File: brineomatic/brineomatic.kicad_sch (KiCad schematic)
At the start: 9 parts, among them J1 Conn_01x04_MountingPin

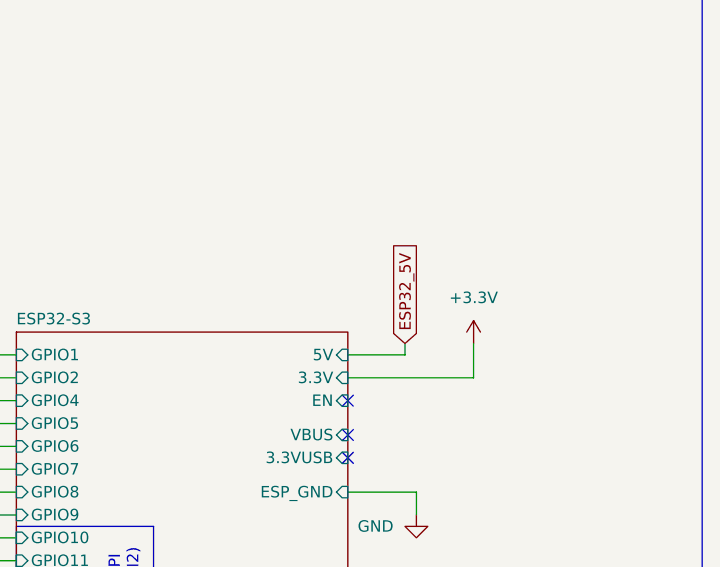
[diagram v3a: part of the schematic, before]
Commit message: 5v power supply is sorted.
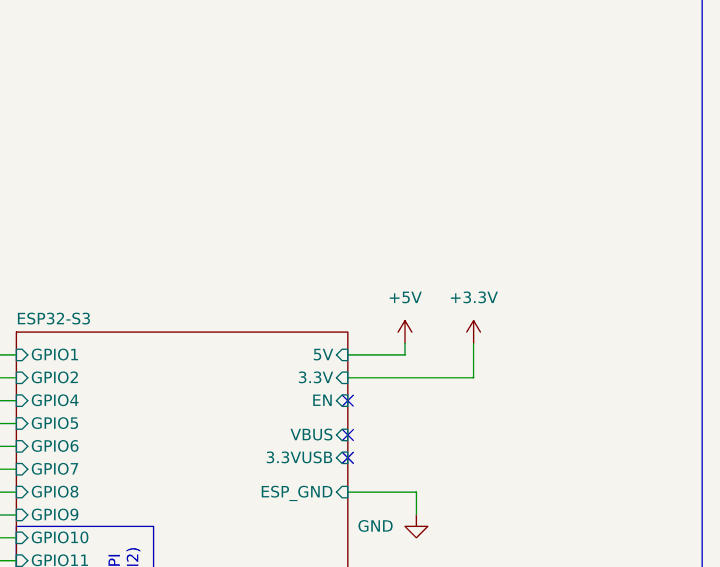
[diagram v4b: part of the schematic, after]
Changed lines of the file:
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@@
 		)
 	)
-	(global_label "ESP32_5V"
+	(global_label "SCL"
 		(shape input)
-		(at 241.3 69.85 90)
+		(at 195.58 96.52 180)
 		(fields_autoplaced yes)
 		(effects
@@
 				(size 1.27 1.27)
 			)
-			(justify left)
+			(justify right)
 		)
 		(property "Intersheetrefs" "${INTERSHEET_REFS}"
-			(at 241.3 57.5516 90)
-			(effects
-				(font
-					(size 1.27 1.27)
-				)
-				(justify left)
-				(hide yes)
-			)
-		)
-	)
-	(global_label "SCL"
+			(at 189.0872 96.52 0)
+			(effects
+				(font
+					(size 1.27 1.27)
+				)
+				(justify right)
+				(hide yes)
+			)
+		)
+	)
+	(global_label "GPIO48"
 		(shape input)
-		(at 195.58 96.52 180)
+		(at 45.72 175.26 0)
 		(fields_autoplaced yes)
 		(effects
@@
 				(size 1.27 1.27)
 			)
-			(justify right)
+			(justify left)
 		)
 		(property "Intersheetrefs" "${INTERSHEET_REFS}"
-			(at 189.0872 96.52 0)
-			(effects
-				(font
-					(size 1.27 1.27)
-				)
-				(justify right)
-				(hide yes)
-			)
-		)
-	)
-	(global_label "GPIO48"
+			(at 55.5995 175.26 0)
+			(effects
+				(font
+					(size 1.27 1.27)
+				)
+				(justify left)
+				(hide yes)
+			)
+		)
+	)
+	(global_label "SOLENOID3"
 		(shape input)
-		(at 45.72 175.26 0)
+		(at 162.56 91.44 0)
 		(fields_autoplaced yes)
 		(effects
@@
 		)
 		(property "Intersheetrefs" "${INTERSHEET_REFS}"
-			(at 55.5995 175.26 0)
+			(at 176.0076 91.44 0)
 			(effects
 				(font
@@
 		)
 	)
-	(global_label "SOLENOID3"
+	(global_label "TMC2209_RX"
 		(shape input)
-		(at 162.56 91.44 0)
+		(at 195.58 88.9 180)
 		(fields_autoplaced yes)
 		(effects
@@
 				(size 1.27 1.27)
 			)
-			(justify left)
+			(justify right)
 		)
 		(property "Intersheetrefs" "${INTERSHEET_REFS}"
-			(at 176.0076 91.44 0)
-			(effects
-				(font
-					(size 1.27 1.27)
-				)
-				(justify left)
-				(hide yes)
-			)
-		)
-	)
-	(global_label "TMC2209_RX"
+			(at 180.6207 88.9 0)
+			(effects
+				(font
+					(size 1.27 1.27)
+				)
+				(justify right)
+				(hide yes)
+			)
+		)
+	)
+	(global_label "GPIO5"
 		(shape input)
-		(at 195.58 88.9 180)
+		(at 195.58 78.74 180)
 		(fields_autoplaced yes)
 		(effects
@@
 		)
 		(property "Intersheetrefs" "${INTERSHEET_REFS}"
-			(at 180.6207 88.9 0)
+			(at 186.91 78.74 0)
 			(effects
 				(font
@@
 		)
 	)
-	(global_label "GPIO5"
+	(global_label "SOLENOID2"
 		(shape input)
-		(at 195.58 78.74 180)
+		(at 195.58 106.68 180)
 		(fields_autoplaced yes)
 		(effects
@@
 		)
 		(property "Intersheetrefs" "${INTERSHEET_REFS}"
-			(at 186.91 78.74 0)
+			(at 182.1324 106.68 0)
 			(effects
 				(font
@@
 		)
 	)
-	(global_label "SOLENOID2"
+	(global_label "SCL"
 		(shape input)
-		(at 195.58 106.68 180)
+		(at 81.28 171.45 180)
 		(fields_autoplaced yes)
 		(effects
@@
 		)
 		(property "Intersheetrefs" "${INTERSHEET_REFS}"
-			(at 182.1324 106.68 0)
+			(at 74.7872 171.45 0)
 			(effects
 				(font
@@
 		)
 	)
-	(global_label "SCL"
+	(global_label "GPIO5"
 		(shape input)
-		(at 81.28 171.45 180)
+		(at 48.26 180.34 0)
 		(fields_autoplaced yes)
 		(effects
@@
 				(size 1.27 1.27)
 			)
-			(justify right)
+			(justify left)
 		)
 		(property "Intersheetrefs" "${INTERSHEET_REFS}"
-			(at 74.7872 171.45 0)
-			(effects
-				(font
-					(size 1.27 1.27)
-				)
-				(justify right)
-				(hide yes)
-			)
-		)
-	)
-	(global_label "GPIO5"
+			(at 56.93 180.34 0)
+			(effects
+				(font
+					(size 1.27 1.27)
+				)
+				(justify left)
+				(hide yes)
+			)
+		)
+	)
+	(global_label "TMC2209_DIR"
 		(shape input)
-		(at 48.26 180.34 0)
+		(at 85.09 46.99 0)
 		(fields_autoplaced yes)
 		(effects
@@
 		)
 		(property "Intersheetrefs" "${INTERSHEET_REFS}"
-			(at 56.93 180.34 0)
+			(at 100.7146 46.99 0)
 			(effects
 				(font
@@
 		)
 	)
-	(global_label "TMC2209_DIR"
+	(global_label "TMC2209_STEP"
 		(shape input)
-		(at 85.09 46.99 0)
+		(at 85.09 44.45 0)
 		(fields_autoplaced yes)
 		(effects
@@
 		)
 		(property "Intersheetrefs" "${INTERSHEET_REFS}"
-			(at 100.7146 46.99 0)
+			(at 102.1659 44.45 0)
 			(effects
 				(font
@@
 		)
 	)
-	(global_label "TMC2209_STEP"
+	(global_label "TMC2209_TX"
 		(shape input)
-		(at 85.09 44.45 0)
+		(at 195.58 91.44 180)
 		(fields_autoplaced yes)
 		(effects
@@
 				(size 1.27 1.27)
 			)
-			(justify left)
+			(justify right)
 		)
 		(property "Intersheetrefs" "${INTERSHEET_REFS}"
-			(at 102.1659 44.45 0)
-			(effects
-				(font
-					(size 1.27 1.27)
-				)
-				(justify left)
+			(at 180.9231 91.44 0)
+			(effects
+				(font
+					(size 1.27 1.27)
+				)
+				(justify right)
 				(hide yes)
 			)
@@
 	(global_label "TMC2209_TX"
 		(shape input)
-		(at 195.58 91.44 180)
+		(at 85.09 58.42 0)
 		(fields_autoplaced yes)
 		(effects
@@
 				(size 1.27 1.27)
 			)
-			(justify right)
+			(justify left)
 		)
 		(property "Intersheetrefs" "${INTERSHEET_REFS}"
-			(at 180.9231 91.44 0)
-			(effects
-				(font
-					(size 1.27 1.27)
-				)
-				(justify right)
-				(hide yes)
-			)
-		)
-	)
-	(global_label "TMC2209_TX"
+			(at 99.7469 58.42 0)
+			(effects
+				(font
+					(size 1.27 1.27)
+				)
+				(justify left)
+				(hide yes)
+			)
+		)
+	)
+	(global_label "TMC2209_DIR"
 		(shape input)
-		(at 85.09 58.42 0)
+		(at 195.58 81.28 180)
 		(fields_autoplaced yes)
 		(effects
@@
 				(size 1.27 1.27)
 			)
-			(justify left)
-		)
-		(property "Intersheetrefs" "${INTERSHEET_REFS}"
-			(at 99.7469 58.42 0)
-			(effects
-				(font
-					(size 1.27 1.27)
-				)
-				(justify left)
-				(hide yes)
-			)
-		)
-	)
-	(global_label "TMC2209_DIR"
-		(shape input)
-		(at 195.58 81.28 180)
-		(fields_autoplaced yes)
-		(effects
-			(font
-				(size 1.27 1.27)
-			)
 			(justify right)
 		)
@@
 					(unit 1)
 				)
+			)
+		)
+	)
+	(symbol
+		(lib_id "power:+5V")
+		(at 241.3 69.85 0)
+		(unit 1)
+		(exclude_from_sim no)
+		(in_bom yes)
+		(on_board yes)
+		(dnp no)
+		(fields_autoplaced yes)
+		(property "Reference" "#PWR012"
+			(at 241.3 73.66 0)
+			(effects
+				(font
+					(size 1.27 1.27)
+				)
+				(hide yes)
+			)
+		)
+		(property "Value" "+5V"
+			(at 241.3 64.77 0)
+			(effects
+				(font
+					(size 1.27 1.27)
+				)
+			)
+		)
+		(property "Footprint" ""
+			(at 241.3 69.85 0)
+			(effects
+				(font
+					(size 1.27 1.27)
+				)
+				(hide yes)
+			)
+		)
+		(property "Datasheet" ""
+			(at 241.3 69.85 0)
+			(effects
+				(font
+					(size 1.27 1.27)
+				)
+				(hide yes)
+			)
+		)
+		(property "Description" "Power symbol creates a global label with name \"+5V\""
+			(at 241.3 69.85 0)
+			(effects
+				(font
+					(size 1.27 1.27)
+				)
+				(hide yes)
+			)
+		)
+		(pin "1"
+		)
+		(instances
+			(project ""
+				(path "/96477ae2-ef08-48f3-8dd4-fe4478541f68"
+					(reference "#PWR012")
+					(unit 1)
+				)

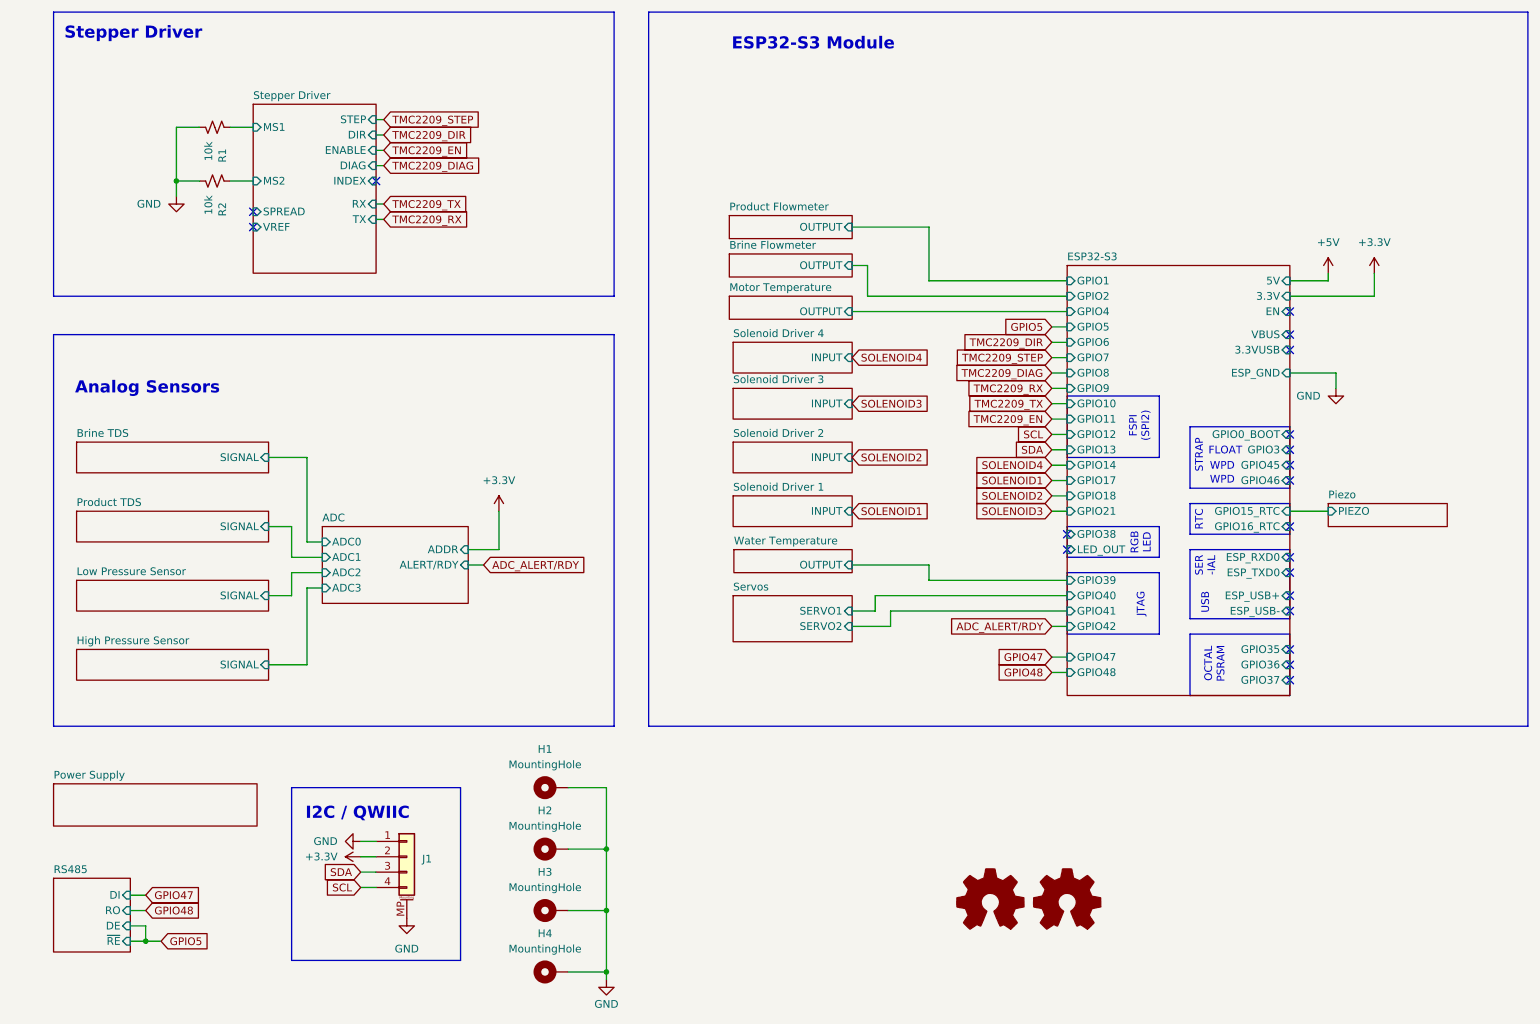
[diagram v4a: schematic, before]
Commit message: stacked tds, removed stepper vref, pulled in esp32-s3 schematic, added extra relay output
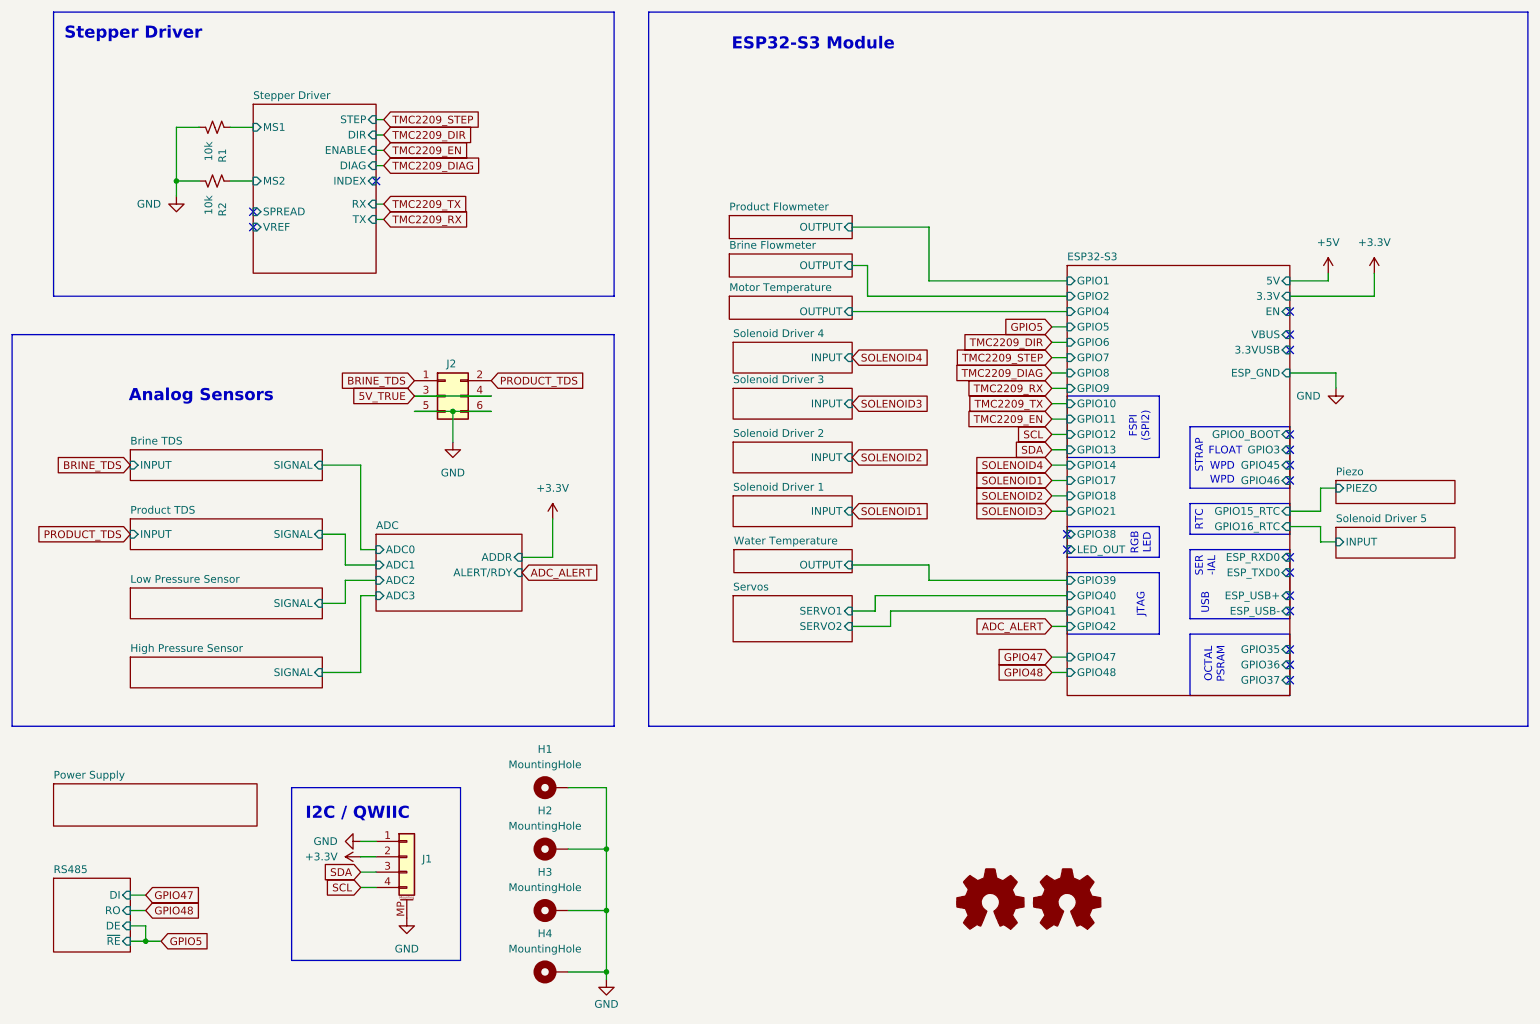
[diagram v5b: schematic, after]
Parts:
- added J2: ~, Connector_PinHeader_2.54mm:PinHeader_2x03_P2.54mm_Horizontal, symbol Connector_Generic:Conn_02x03_Odd_Even
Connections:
- net GND: now also J2.5 (Pin_5), J2.6 (Pin_6)
- new net 5V_TRUE: J2.3 (Pin_3), J2.4 (Pin_4)
- new net BRINE_TDS: J2.1 (Pin_1)
- new net PRODUCT_TDS: J2.2 (Pin_2)
- no-connect marks 20 -> 19
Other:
- added sheet Solenoid Driver 5 (solenoid_driver.kicad_sch)
- sheet Brine TDS ports: added INPUT; removed none
- sheet Product TDS ports: added INPUT; removed none

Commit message: all connectors are now flush withe 3mm outside edge of the case
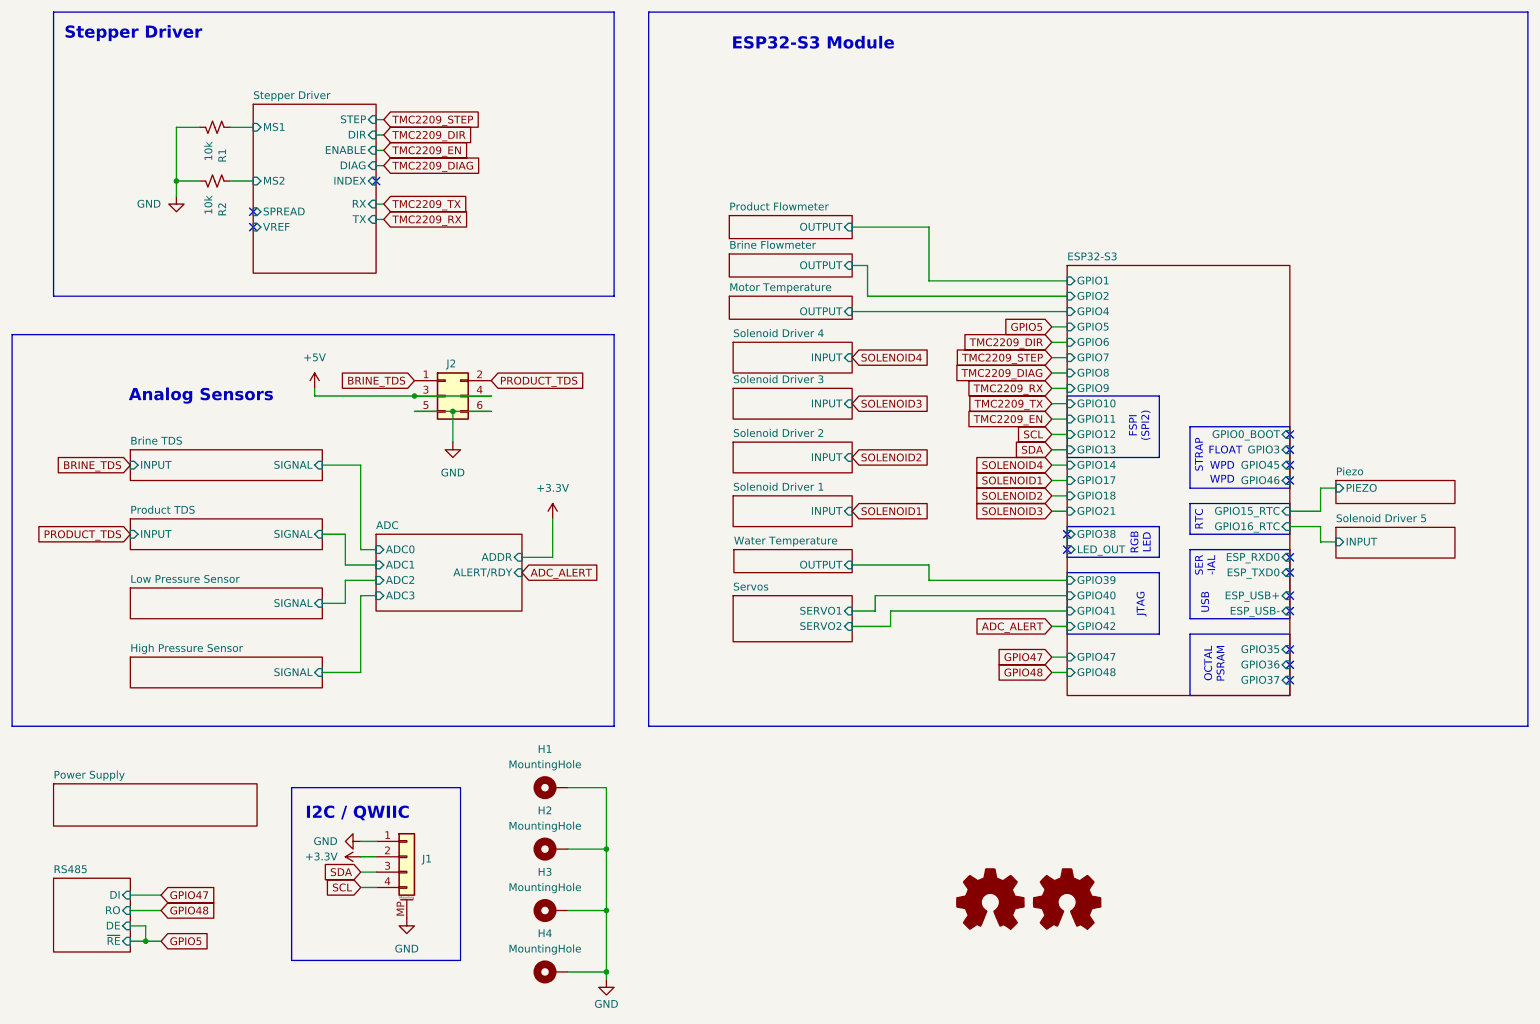
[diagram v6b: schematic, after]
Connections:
- net 5V_TRUE is gone; now on net +5V: J2.3 (Pin_3), J2.4 (Pin_4)
- no-connect marks 19 -> 16
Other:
- sheet ESP32-S3 ports: added none; removed 3.3V, 3.3VUSB, 5V, EN, ESP_GND, VBUS

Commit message: schematic tidy, usb c position verified, component placement work.
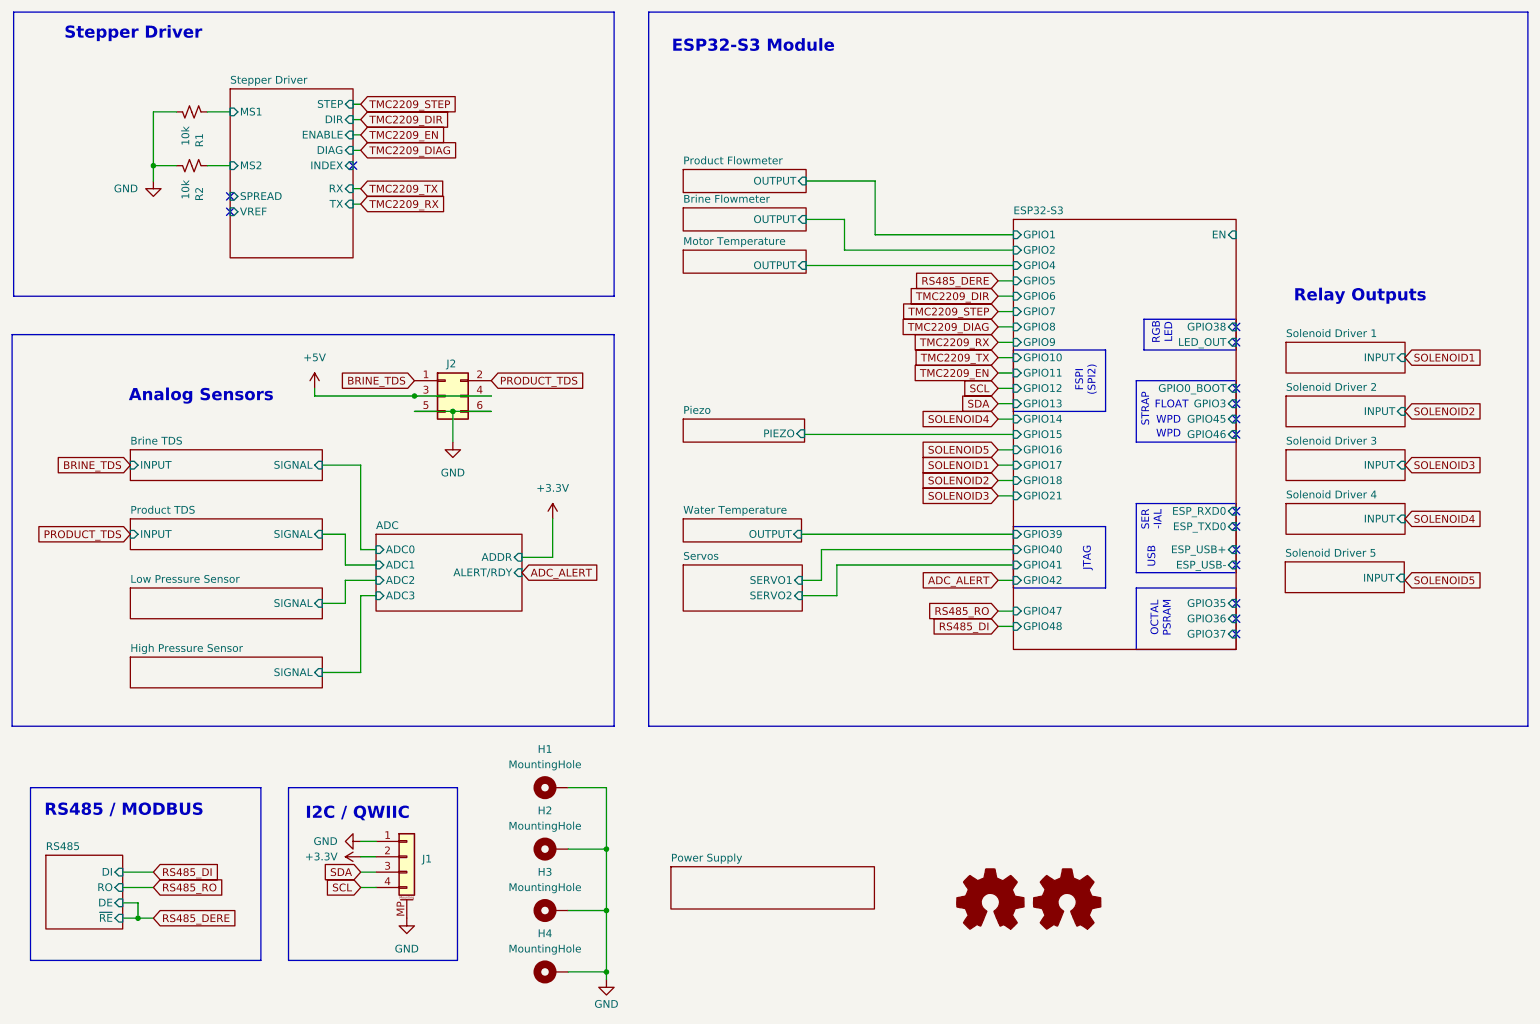
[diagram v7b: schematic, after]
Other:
- sheet ESP32-S3 ports: added EN, GPIO15, GPIO16; removed GPIO15_RTC, GPIO16_RTC
- note added: "RS485 / MODBUS"
- note added: "Relay Outputs"
- note removed: "RTC"
- moved on the sheet: R1, R2
